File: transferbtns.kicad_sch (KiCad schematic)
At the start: 23 parts, among them J1 8P8C, J2 8P8C, U6 74LS165

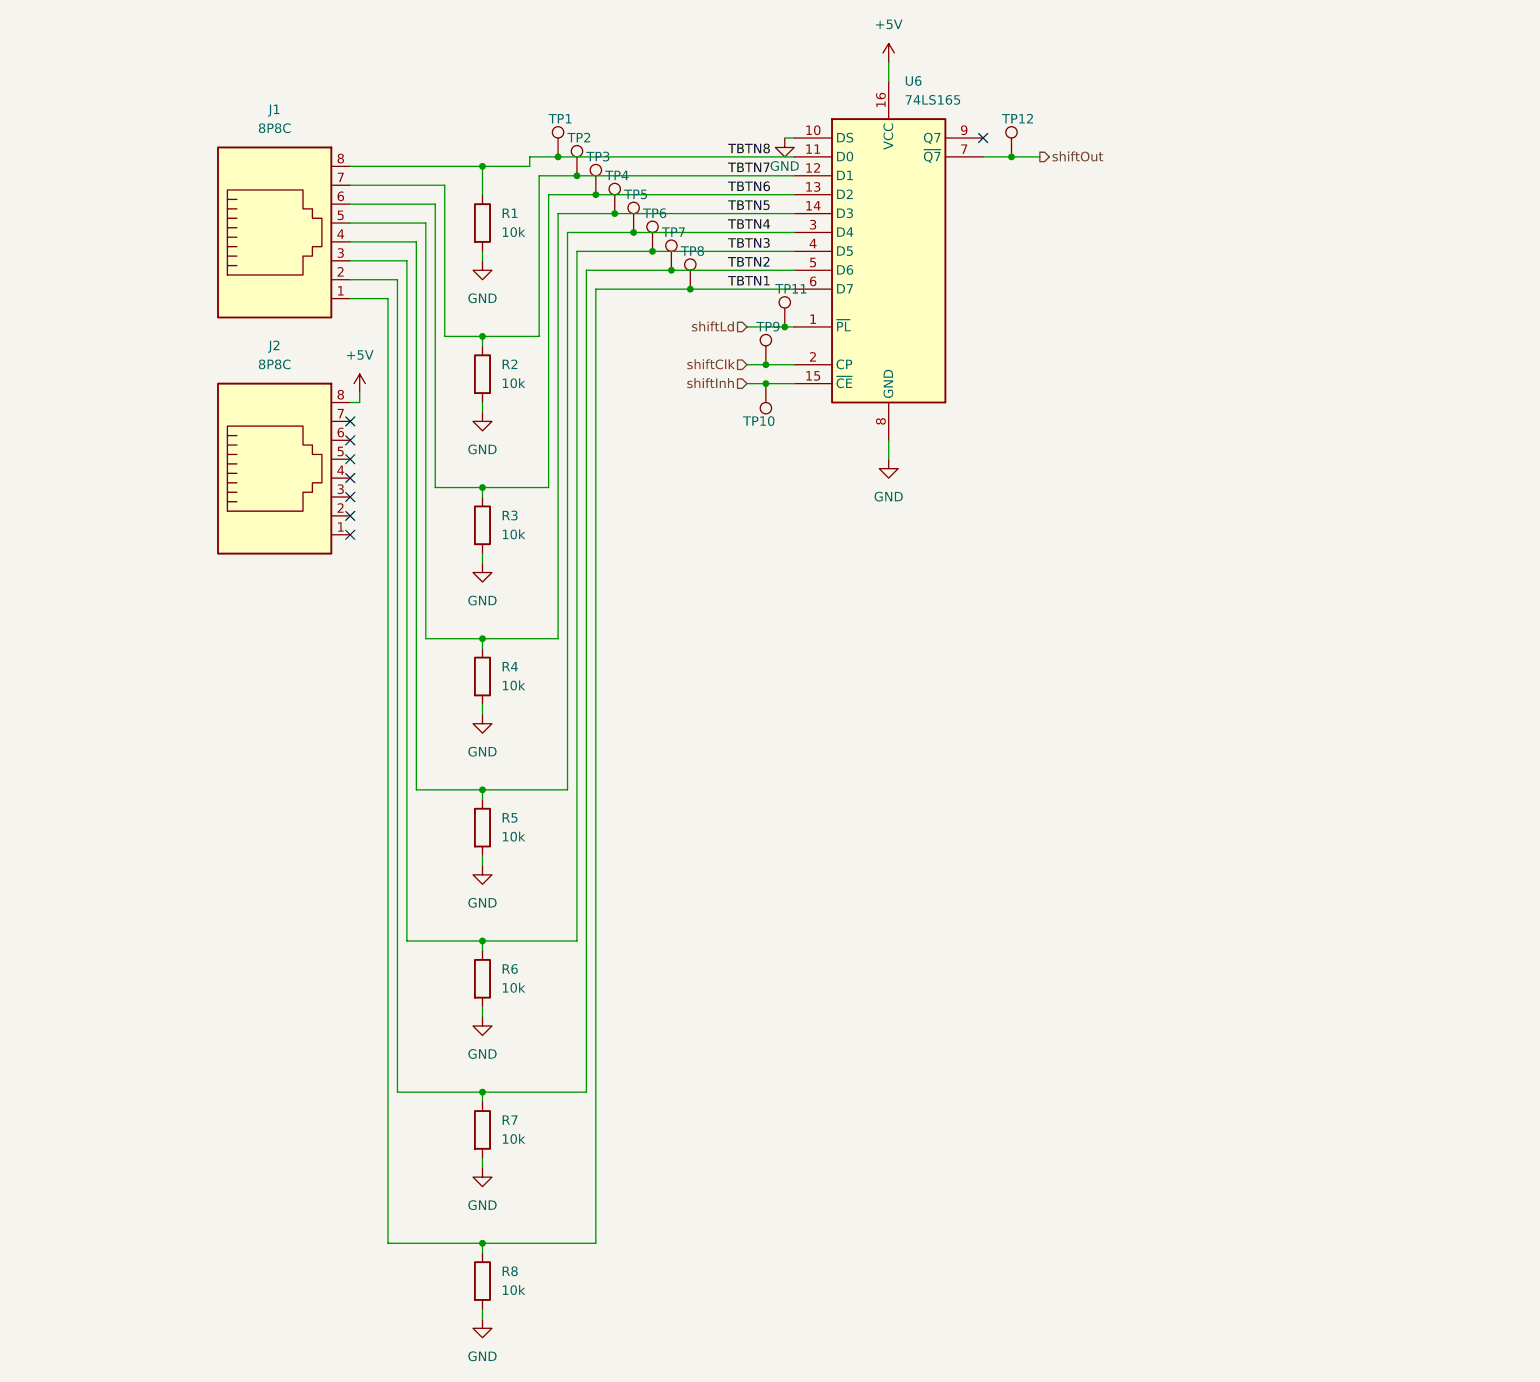
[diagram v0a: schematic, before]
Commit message: added power mux, finished up schematic and picking footprints/partnumbers
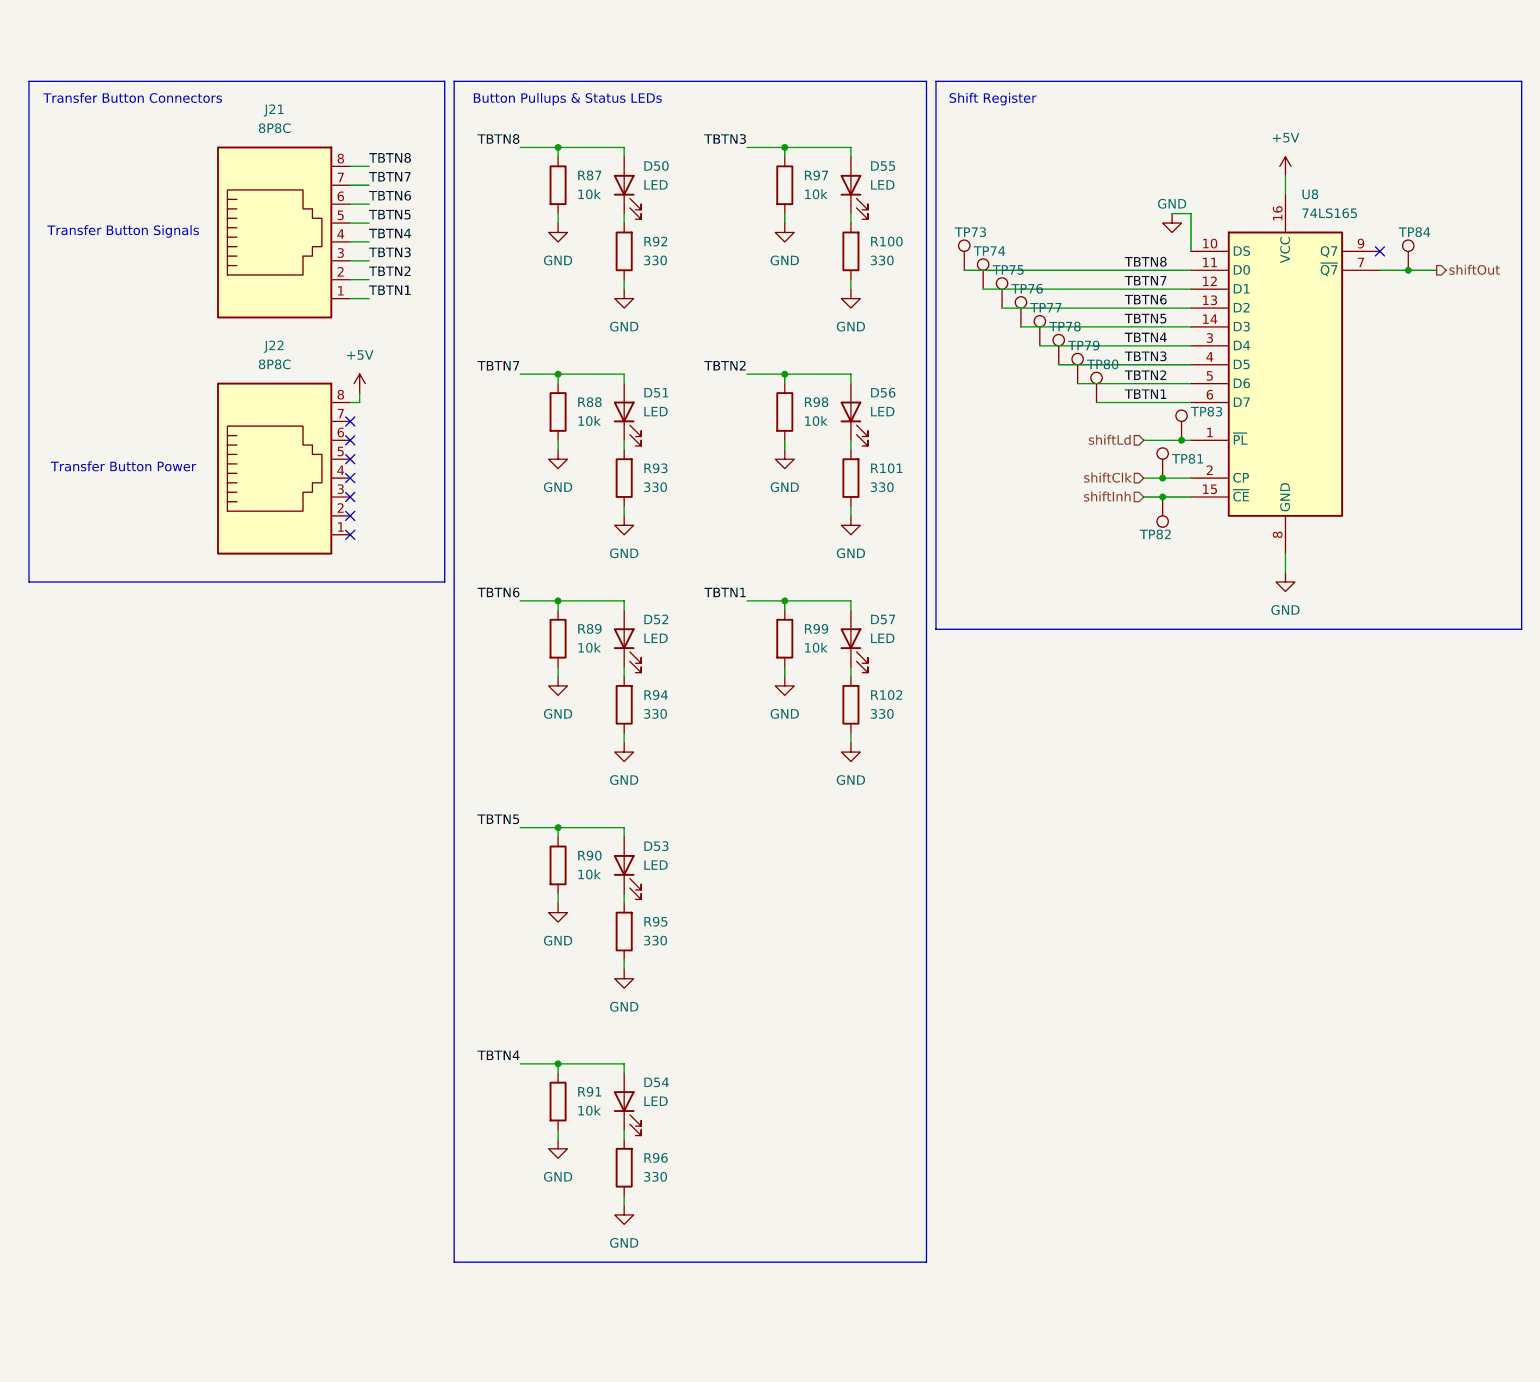
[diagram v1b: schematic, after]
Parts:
- removed R1, R2, R3, R4, R5, R6, R7, R8: 10k, Resistor_SMD:R_0805_2012Metric, symbol Device:R
- added D50, D51, D52, D53, D54, D55, D56, D57: LED, Resistor_SMD:R_0603_1608Metric, symbol Device:LED
- added R100, R101, R102, R92, R93, R94, R95, R96: 330, Resistor_SMD:R_0805_2012Metric, symbol Device:R
- added R87, R88, R89, R90, R91, R97, R98, R99: 10k, symbol Device:R
- U8: renamed from U6; footprint Package_DIP:DIP-16_W7.62mm -> Package_SO:TSSOP-16_4.4x5mm_P0.65mm; DKPN 296-14885-5-ND -> 296-8253-1-ND
- renumbered J1 to J21, J2 to J22, TP1 to TP73, TP2 to TP74, TP3 to TP75, TP4 to TP76, TP5 to TP77, TP6 to TP78, TP7 to TP79, TP8 to TP80, TP9 to TP81, TP10 to TP82, TP11 to TP83, TP12 to TP84
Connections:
- net GND: now also R100.1, R101.1, R102.1, R87.2, R88.2, R89.2, R90.2, R91.2, R92.1, R93.1, R94.1, R95.1, R96.1, R97.2, R98.2, R99.2
- net TBTN1: now also D57.2 (A), R99.1
- net TBTN2: now also D56.2 (A), R98.1
- net TBTN3: now also D55.2 (A), R97.1
- net TBTN4: now also D54.2 (A), R91.1
- net TBTN5: now also D53.2 (A), R90.1
- net TBTN6: now also D52.2 (A), R89.1
- net TBTN7: now also D51.2 (A), R88.1
- net TBTN8: now also D50.2 (A), R87.1
- new net: D54.1 (K), R96.2
- new net: D56.1 (K), R101.2
- new net: D57.1 (K), R102.2
- new net: D51.1 (K), R93.2
- new net: D53.1 (K), R95.2
- new net: D55.1 (K), R100.2
- new net: D50.1 (K), R92.2
- new net: D52.1 (K), R94.2
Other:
- note added: "Button Pullups & Status LEDs"
- note added: "Shift Register"
- note added: "Transfer Button Connectors"
- note added: "Transfer Button Power"
- note added: "Transfer Button Signals"
- moved on the sheet: TP73, TP74, TP75, TP76, TP77, TP78, TP79, TP80, TP81, TP82, TP83, TP84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

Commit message: forgot to add footprints for 10k resistors
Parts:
- R87, R88, R89, R90, R91, R97, R98, R99: footprint (none) -> Resistor_SMD:R_0805_2012Metric
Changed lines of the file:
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@@
 			)
 		)
-		(property "Footprint" ""
+		(property "Footprint" "Resistor_SMD:R_0805_2012Metric"
 			(at 93.472 68.58 90)
 			(hide yes)
@@
 			)
 		)
-		(property "Footprint" ""
+		(property "Footprint" "Resistor_SMD:R_0805_2012Metric"
 			(at 93.472 129.54 90)
 			(hide yes)
@@
 			)
 		)
-		(property "Footprint" ""
+		(property "Footprint" "Resistor_SMD:R_0805_2012Metric"
 			(at 93.472 161.29 90)
 			(hide yes)
@@
 			)
 		)
-		(property "Footprint" ""
+		(property "Footprint" "Resistor_SMD:R_0805_2012Metric"
 			(at 93.472 38.1 90)
 			(hide yes)
@@
 			)
 		)
-		(property "Footprint" ""
+		(property "Footprint" "Resistor_SMD:R_0805_2012Metric"
 			(at 93.472 99.06 90)
 			(hide yes)
@@
 			)
 		)
-		(property "Footprint" ""
+		(property "Footprint" "Resistor_SMD:R_0805_2012Metric"
 			(at 123.952 68.58 90)
 			(hide yes)
@@
 			)
 		)
-		(property "Footprint" ""
+		(property "Footprint" "Resistor_SMD:R_0805_2012Metric"
 			(at 123.952 38.1 90)
 			(hide yes)
@@
 			)
 		)
-		(property "Footprint" ""
+		(property "Footprint" "Resistor_SMD:R_0805_2012Metric"
 			(at 123.952 99.06 90)
 			(hide yes)
